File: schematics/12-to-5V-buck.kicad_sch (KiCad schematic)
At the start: 12 parts, among them U2 TPS54308

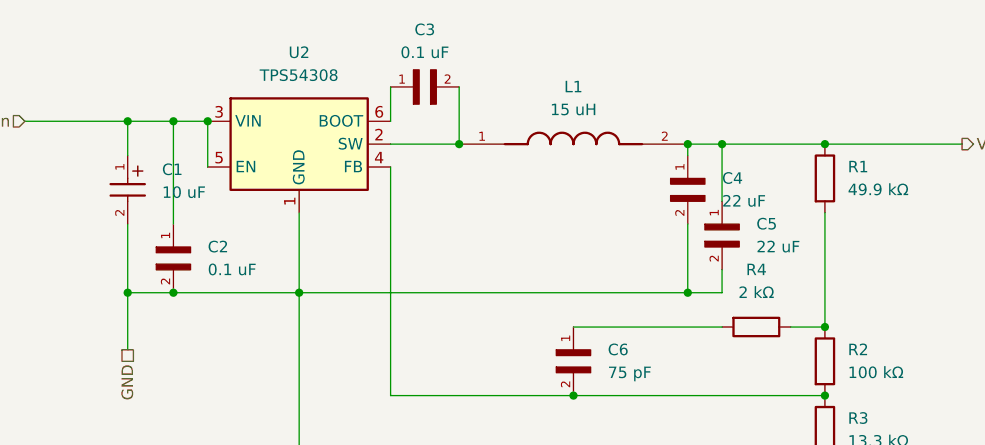
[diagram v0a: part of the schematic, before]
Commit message: Added accelerometer + gyroscope
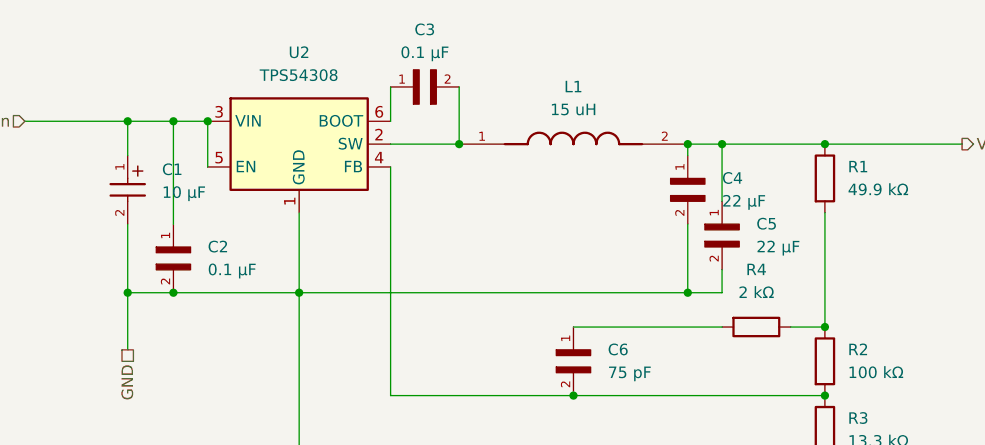
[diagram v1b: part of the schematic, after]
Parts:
- C1: value 10 uF -> 10 µF
- C2, C3: value 0.1 uF -> 0.1 µF
- C4, C5: value 22 uF -> 22 µF
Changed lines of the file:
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@@
 			)
 		)
-		(property "Value" "22 uF"
+		(property "Value" "22 µF"
 			(at 115.57 54.6099 90)
 			(effects
@@
 			)
 		)
-		(property "Value" "0.1 uF"
+		(property "Value" "0.1 µF"
 			(at 54.61 57.1499 90)
 			(effects
@@
 			)
 		)
-		(property "Value" "10 uF"
+		(property "Value" "10 µF"
 			(at 49.53 48.563 90)
 			(effects
@@
 			)
 		)
-		(property "Value" "22 uF"
+		(property "Value" "22 µF"
 			(at 111.76 49.5299 90)
 			(effects
@@
 			)
 		)
-		(property "Value" "0.1 uF"
+		(property "Value" "0.1 µF"
 			(at 78.74 33.02 0)
 			(effects

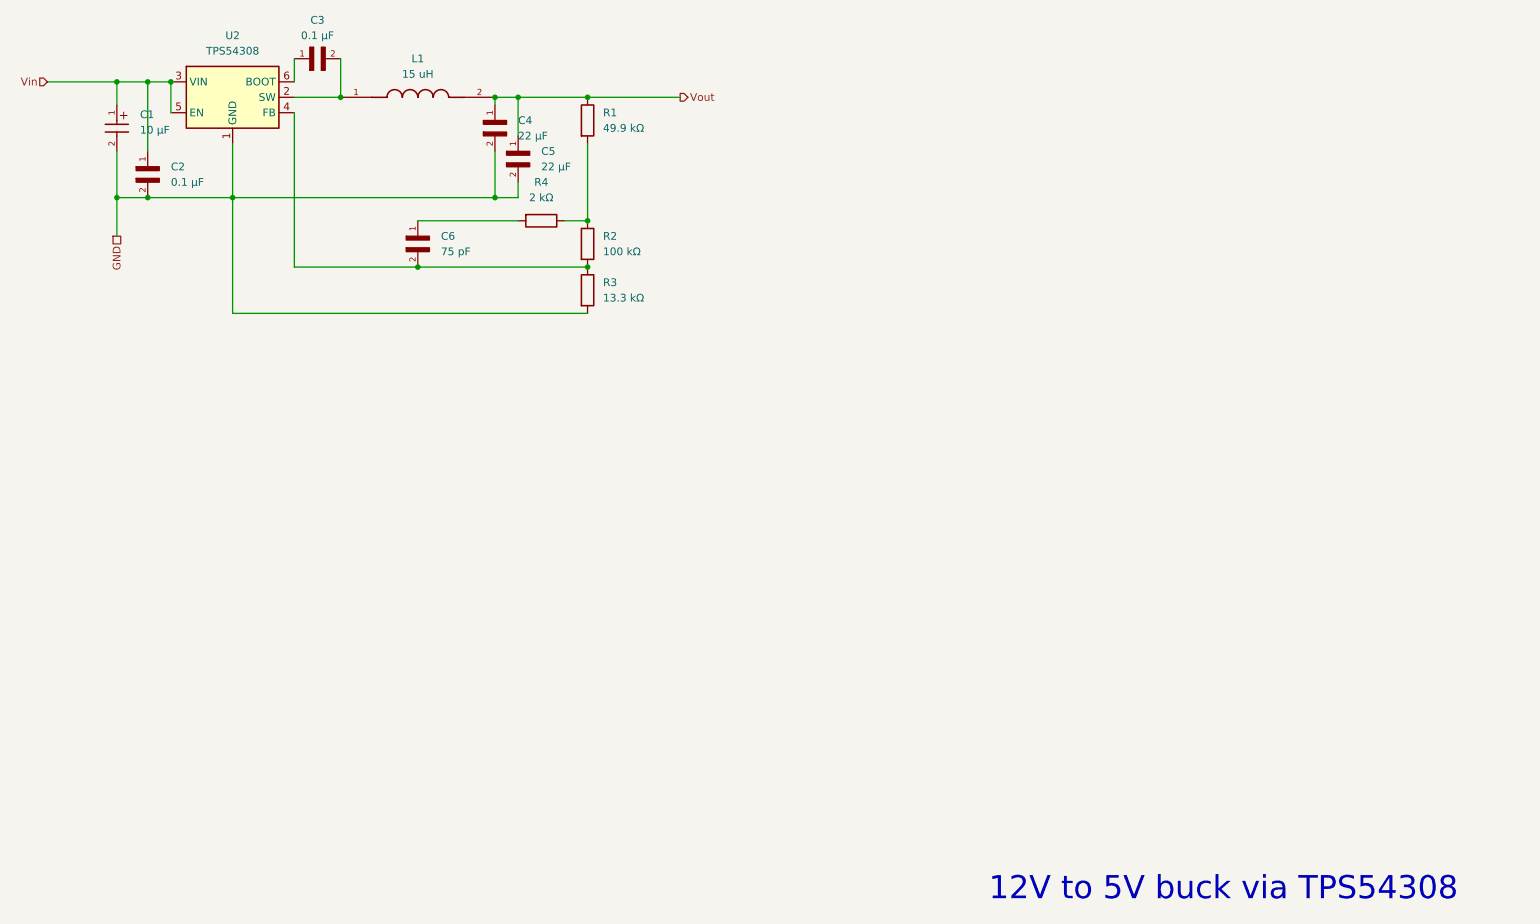
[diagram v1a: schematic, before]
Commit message: Normalized sheet titles; added MMCX connector for GPS antenna + active antenna power switch
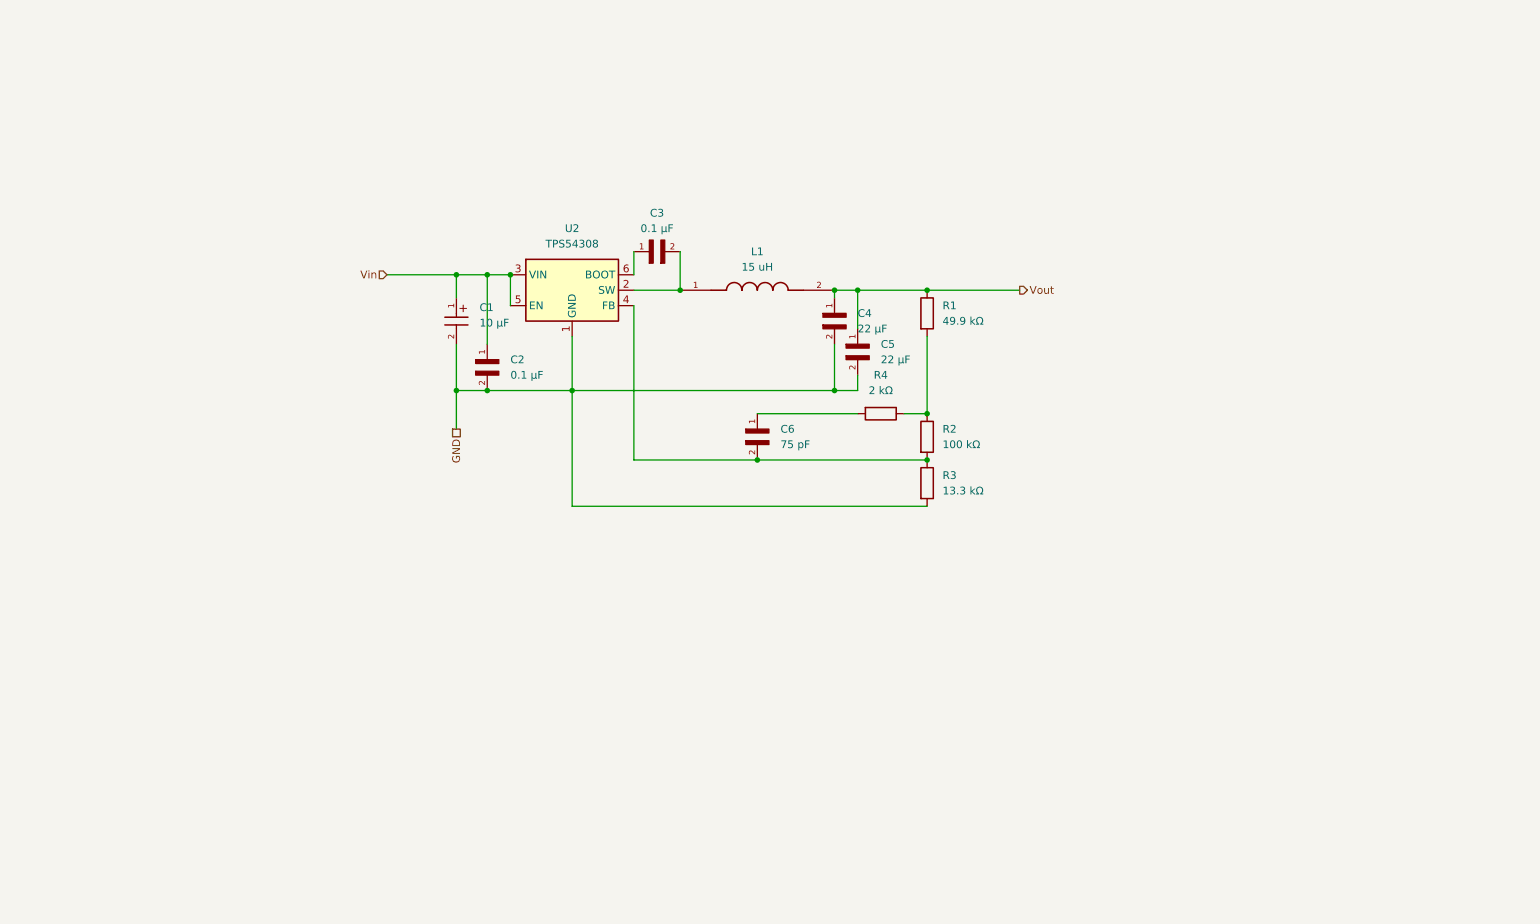
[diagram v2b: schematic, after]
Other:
- note removed: "12V to 5V buck via TPS54308"
- title: (none) -> 12V to 5V buck via TPS54308
- moved on the sheet: C1, C2, C3, C4, C5, C6, L1, R1, R2, R3, R4, U2

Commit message: Small schema refactor
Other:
- title: 12V to 5V buck via TPS54308 -> 12V CC / 5V CC buck via TPS54308
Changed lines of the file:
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@@
 	(paper "A4")
 	(title_block
-		(title "12V to 5V buck via TPS54308")
+		(title "12V CC / 5V CC buck via TPS54308")
 	)
 	(junction

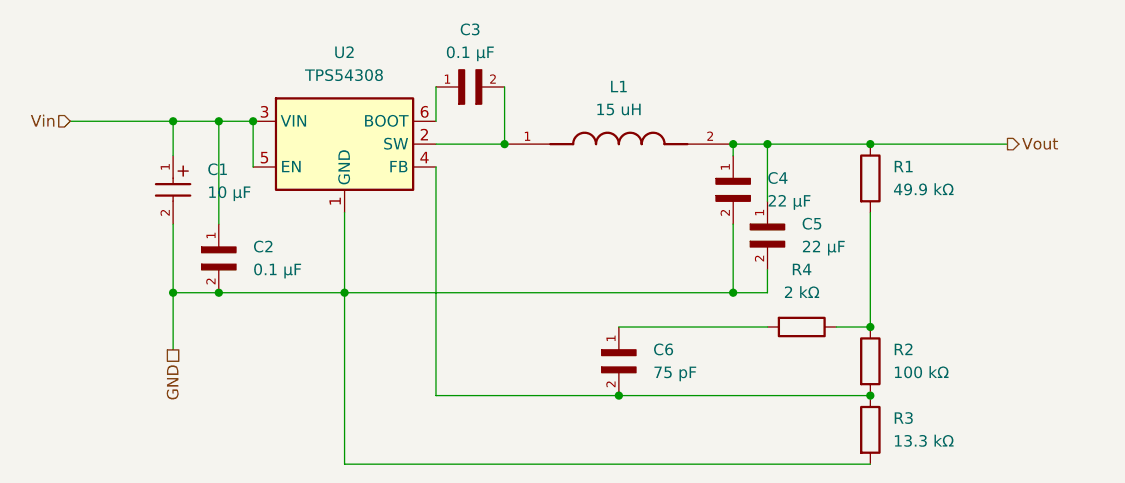
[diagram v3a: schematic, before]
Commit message: Include GND in each schema sub-pages
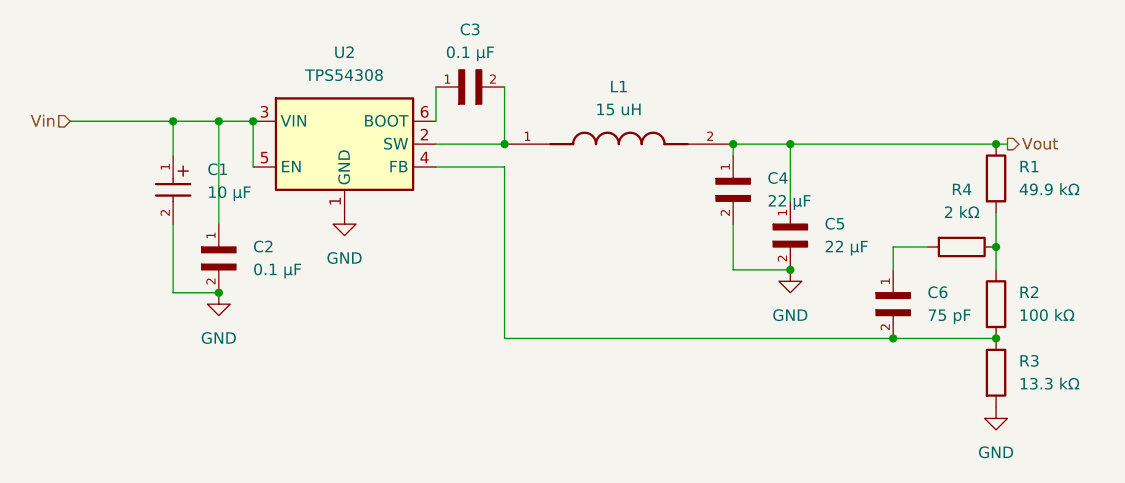
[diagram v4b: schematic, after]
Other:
- moved on the sheet: C5, C6, R1, R2, R3, R4

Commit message: Refactor WIP
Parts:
- R1, R2, R3, R4: footprint (none) -> Resistor_SMD:R_0603_1608Metric
- renumbered U2 to U1
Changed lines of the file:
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@@
 			)
 		)
-		(property "Footprint" ""
+		(property "Footprint" "Resistor_SMD:R_0603_1608Metric"
 			(at 189.23 84.582 90)
 			(effects
@@
 			)
 		)
-		(property "Footprint" ""
+		(property "Footprint" "Resistor_SMD:R_0603_1608Metric"
 			(at 191.262 78.74 90)
 			(effects
@@
 			)
 		)
-		(property "Footprint" ""
+		(property "Footprint" "Resistor_SMD:R_0603_1608Metric"
 			(at 191.262 92.71 90)
 			(effects
@@
 			)
 		)
-		(property "Footprint" ""
+		(property "Footprint" "Resistor_SMD:R_0603_1608Metric"
 			(at 191.262 100.33 90)
 			(effects
@@
 		(dnp no)
 		(fields_autoplaced yes)
-		(property "Reference" "U2"
+		(property "Reference" "U1"
 			(at 120.65 64.77 0)
 			(effects
@@
 		)
 		(property "Description" "3A, 4.5 to 28V Input, EMI Friendly integrated switch synchronous step-down regulator, continuous-conduction, SOT-23-6"
+			(at 120.65 74.93 0)
+			(effects
+				(font
+					(size 1.27 1.27)
+				)
+				(hide yes)
+			)
+		)
+		(property "Sim.Library" "libraries/SPICE/TPS54308_TRANS.LIB"
+			(at 120.65 74.93 0)
+			(effects
+				(font
+					(size 1.27 1.27)
+				)
+				(hide yes)
+			)
+		)
+		(property "Sim.Name" "TPS54308_TRANS"
 			(at 120.65 74.93 0)
 			(effects
@@
 			(project "bike-sensors-logger"
 				(path "/2c1d9222-af16-428b-85a5-a3d420373d70/49def333-5dd9-480f-a077-de948f7f462b"
-					(reference "U2")
+					(reference "U1")
 					(unit 1)
 				)

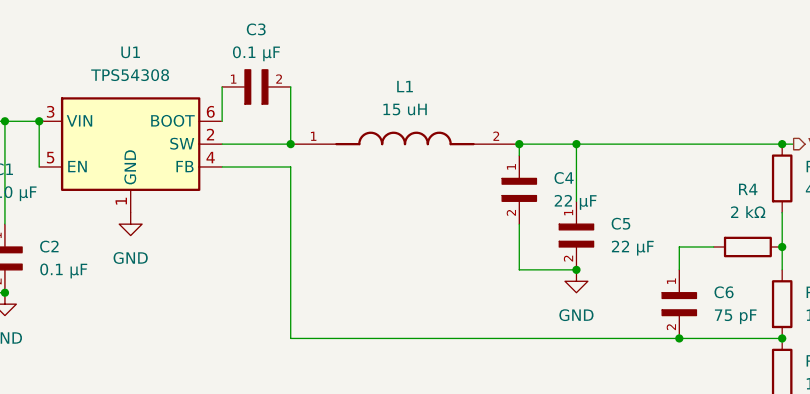
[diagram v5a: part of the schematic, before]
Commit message: Value unit small fix
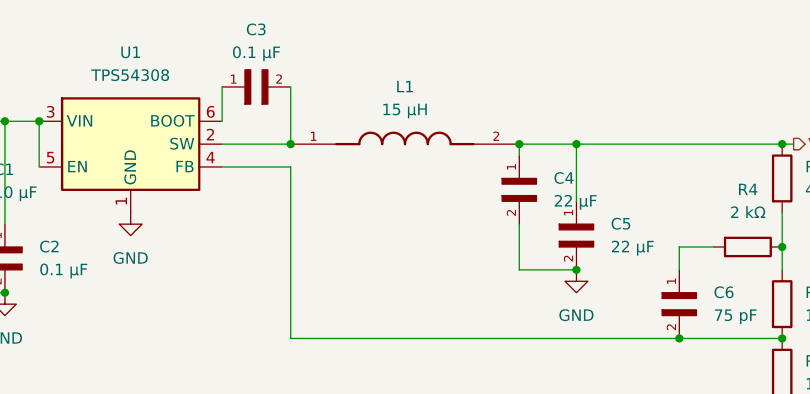
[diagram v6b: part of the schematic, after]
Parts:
- L1: value 15 uH -> 15 µH
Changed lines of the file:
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@@
 			)
 		)
-		(property "Value" "15 uH"
+		(property "Value" "15 µH"
 			(at 151.13 71.12 0)
 			(effects

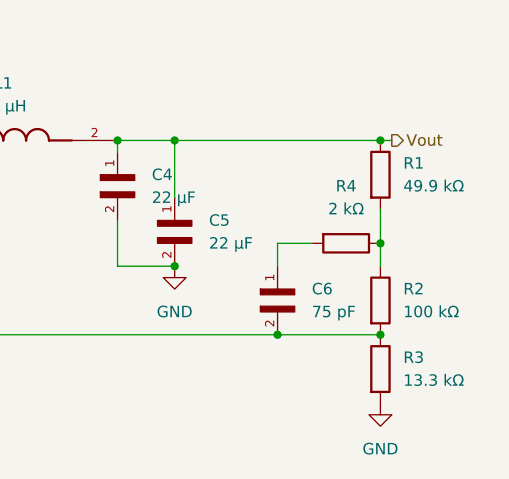
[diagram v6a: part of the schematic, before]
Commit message: Added OBD II connection + OBD II termination check; library scaffolding refactor
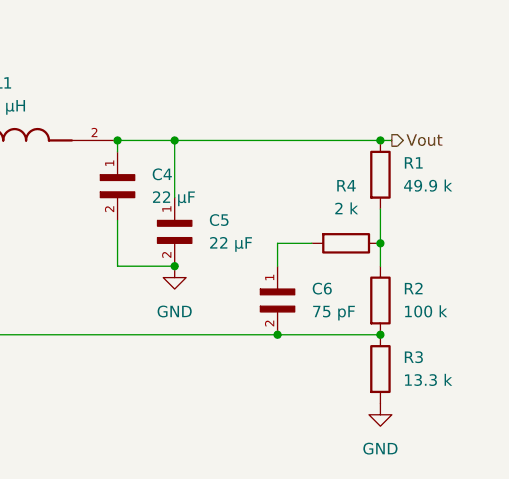
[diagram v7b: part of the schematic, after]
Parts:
- R1: value 49.9 kΩ -> 49.9 k
- R2: value 100 kΩ -> 100 k
- R3: value 13.3 kΩ -> 13.3 k
- R4: value 2 kΩ -> 2 k
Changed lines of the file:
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@@
 			)
 		)
-		(property "Value" "2 kΩ"
+		(property "Value" "2 k"
 			(at 189.23 82.55 90)
 			(effects
@@
 			)
 		)
-		(property "Value" "49.9 kΩ"
+		(property "Value" "49.9 k"
 			(at 195.58 80.0099 0)
 			(effects
@@
 			)
 		)
-		(property "Value" "100 kΩ"
+		(property "Value" "100 k"
 			(at 195.58 93.9799 0)
 			(effects
@@
 			)
 		)
-		(property "Value" "13.3 kΩ"
+		(property "Value" "13.3 k"
 			(at 195.58 101.5999 0)
 			(effects
